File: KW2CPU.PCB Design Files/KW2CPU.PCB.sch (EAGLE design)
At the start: 67 parts, among them IC1 25AA080SN, J1 DF12_M, J2 MOLEX55560-0207, J3 MMCX_VERT, U1 MKW21D, U3 RF6555, U5 F-ANTENNA, X1 32KHZ, X2 32MHZ

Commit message: Added part numbers and manufacturers (inconsistent)
Also moved files to proper directories. Needs manual inconsistency
fixing
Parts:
- C1, C2, C3, C4: MFGN (none) -> Murata; MFGP (none) -> GRM1555C1H120JA01D
- C10, C13, C18, C7: MFGN (none) -> Murata; MFGP (none) -> GRM1555C1H5R0BA01D
- C11, C14, C17, C6: MFGN (none) -> Murata; MFGP (none) -> GRM155R71H102KA01D
- C12, C8: MFGN (none) -> Murata; MFGP (none) -> GRM155R61A334KE15D
- C15, C16, C19, C5: MFGN (none) -> Murata; MFGP (none) -> GRM155R71C104KA88D
- C20: value (none) -> 1.2pF
- C21, C28, C29, C30: value (none) -> 8pF
- C22: value (none) -> 1uF
- C23: value (none) -> 5.1pF
- C25: value (none) -> 0.2pF; MFGN (none) -> Johanson; MFGP (none) -> 500R07S0R2BV4T; NOTES DNP -> (none)
- C26: NOTE DNP -> (none); NOTES (none) -> DNP
- C9: MFGN (none) -> Murata; MFGP (none) -> GRM1555C1H330JA01D
- IC1: MFGN (none) -> Microchip; MFGP (none) -> 25AA640A; MPN (none) -> 25AA640A
- J1: MFGN (none) -> Hirose; MFGP (none) -> DF12(3.0)-40DS-0.5V(86)
- J2: MFGN (none) -> MOLEX; MFGP (none) -> 55560-0207
- L1, L2: value (none) -> 1nH
- L3: value (none) -> 100Ohm Ferrite
- L4: value (none) -> 2.2nH; MFGN (none) -> Murata; MFGP (none) -> LQP15MN2N2B02D
- L5: value (none) -> 0; MFGN (none) -> Panasonic; MFGP (none) -> ERJ-2GE0R00X
- R1: MFGN (none) -> Panasonic; MFGP (none) -> ERJ-2GEJ105X
- R10, R11, R12: MFGN (none) -> Panasonic; MFGP (none) -> ERJ-2RKF1002X
- R4, R5: value (none) -> 0
- R6: value (none) -> 51k
- R7, R9: value (none) -> 0; MFGP ERJ-2GEJ513X -> ERJ-2GE0R00X
- R8: value (none) -> 0; MFGP ERJ-2GEJ513X -> ERJ-2GE0R00X; NOTES (none) -> DNP
- TP1, TP10, TP11, TP12, TP2, TP3, TP4, TP5, TP6, TP7, TP8, TP9, U5: NOTES (none) -> DNP
- U1: MFGN (none) -> Freescale; MFGP (none) -> MKW21D256
- U4: MFGN (none) -> Microchip; MFGP (none) -> MCP1804T-3302I
- X1: MFGN (none) -> EPSON; MFGP (none) -> FC-135 32.7680KA-A3

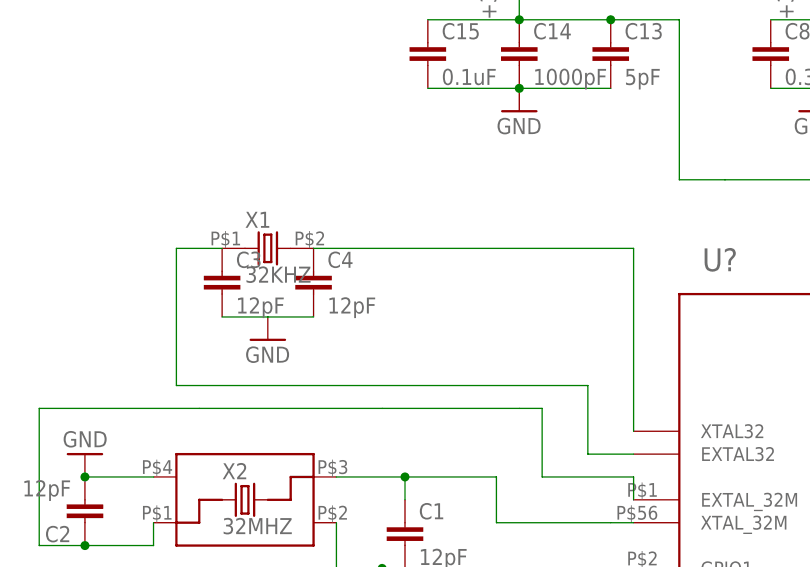
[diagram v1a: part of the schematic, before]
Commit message: Exporting production files in progress
Creating production files. Missing: ECO, Stackup, Drill
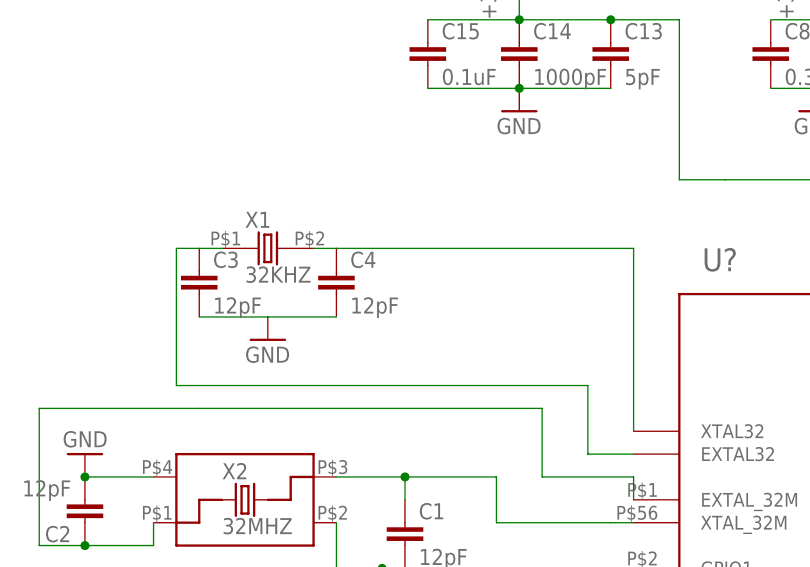
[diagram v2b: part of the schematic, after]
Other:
- moved on the sheet: C3, C4
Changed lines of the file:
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@@
 <attribute name="MFGP" x="-106.68" y="55.88" size="1.778" layer="96" display="off"/>
 </instance>
-<instance part="C3" gate="G$1" x="-111.76" y="53.34">
-<attribute name="MFGN" x="-111.76" y="53.34" size="1.778" layer="96" display="off"/>
-<attribute name="MFGP" x="-111.76" y="53.34" size="1.778" layer="96" display="off"/>
-</instance>
-<instance part="C4" gate="G$1" x="-101.6" y="53.34">
-<attribute name="MFGN" x="-101.6" y="53.34" size="1.778" layer="96" display="off"/>
-<attribute name="MFGP" x="-101.6" y="53.34" size="1.778" layer="96" display="off"/>
+<instance part="C3" gate="G$1" x="-114.3" y="53.34">
+<attribute name="MFGN" x="-114.3" y="53.34" size="1.778" layer="96" display="off"/>
+<attribute name="MFGP" x="-114.3" y="53.34" size="1.778" layer="96" display="off"/>
+</instance>
+<instance part="C4" gate="G$1" x="-99.06" y="53.34">
+<attribute name="MFGN" x="-99.06" y="53.34" size="1.778" layer="96" display="off"/>
+<attribute name="MFGP" x="-99.06" y="53.34" size="1.778" layer="96" display="off"/>
 </instance>
 <instance part="GND33" gate="1" x="-106.68" y="45.72"/>
@@
 <wire x1="-71.12" y1="40.64" x2="-116.84" y2="40.64" width="0.1524" layer="91"/>
 <wire x1="-116.84" y1="40.64" x2="-116.84" y2="55.88" width="0.1524" layer="91"/>
-<wire x1="-116.84" y1="55.88" x2="-111.76" y2="55.88" width="0.1524" layer="91"/>
+<wire x1="-116.84" y1="55.88" x2="-114.3" y2="55.88" width="0.1524" layer="91"/>
+<wire x1="-114.3" y1="55.88" x2="-111.76" y2="55.88" width="0.1524" layer="91"/>
 </segment>
 </net>
@@
 <pinref part="X1" gate="G$1" pin="2"/>
 <pinref part="C4" gate="G$1" pin="1"/>
-<wire x1="-101.6" y1="55.88" x2="-66.04" y2="55.88" width="0.1524" layer="91"/>
+<wire x1="-99.06" y1="55.88" x2="-66.04" y2="55.88" width="0.1524" layer="91"/>
 <pinref part="U1" gate="G$1" pin="XTAL32"/>
 <wire x1="-66.04" y1="55.88" x2="-66.04" y2="35.56" width="0.1524" layer="91"/>
+<wire x1="-99.06" y1="55.88" x2="-101.6" y2="55.88" width="0.1524" layer="91"/>
 </segment>
 </net>
@@
 <pinref part="GND33" gate="1" pin="GND"/>
 <pinref part="C4" gate="G$1" pin="2"/>
-<wire x1="-106.68" y1="48.26" x2="-101.6" y2="48.26" width="0.1524" layer="91"/>
+<wire x1="-106.68" y1="48.26" x2="-99.06" y2="48.26" width="0.1524" layer="91"/>
 <pinref part="C3" gate="G$1" pin="2"/>
-<wire x1="-106.68" y1="48.26" x2="-111.76" y2="48.26" width="0.1524" layer="91"/>
+<wire x1="-106.68" y1="48.26" x2="-114.3" y2="48.26" width="0.1524" layer="91"/>
 </segment>
 <segment>
@@
 </sheet>
 </sheets>
+<errors>
+</errors>
 </schematic>
 </drawing>

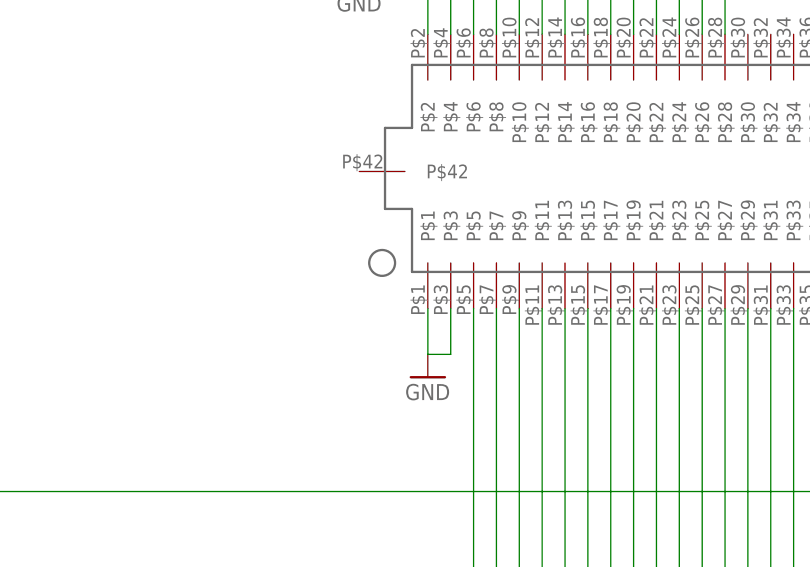
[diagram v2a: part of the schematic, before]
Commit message: KW2CPU.PCB.v1.1 Release
Fixed Gerbers (omitted layer), fixed BOM suffixes (see ECO), tented vias
and antenna holes in Eagle (and Gerbers), added Stackup -> Layer in Fab
notes.
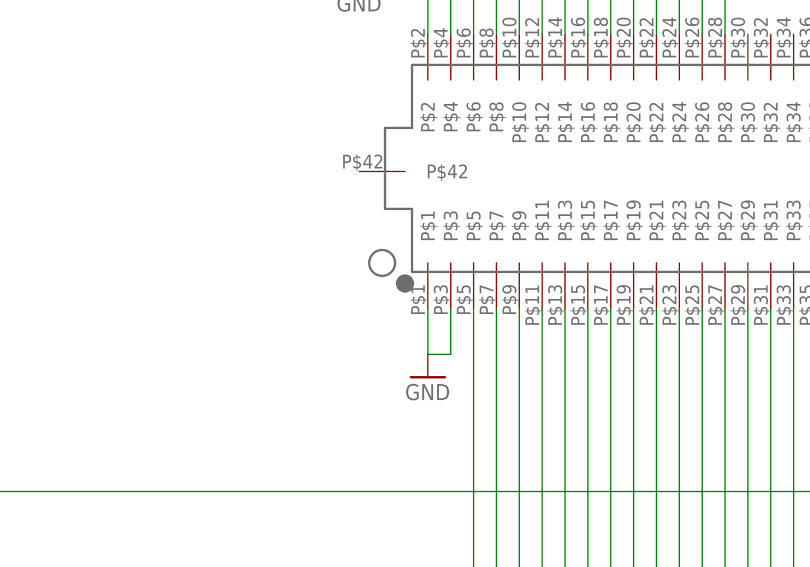
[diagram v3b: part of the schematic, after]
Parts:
- IC1: MFGP 25AA640A -> 25AA640A-I/SN
- U1: MFGP MKW21D256 -> MKW21D256VHA5
- U4: MFGP MCP1804T-3302I -> MCP1804T-3302I/DB
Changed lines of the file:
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@@
 <part name="U1" library="ZIGBEE" deviceset="MKW21D" device="">
 <attribute name="MFGN" value="Freescale"/>
-<attribute name="MFGP" value="MKW21D256"/>
+<attribute name="MFGP" value="MKW21D256VHA5"/>
 </part>
 <part name="GND1" library="supply1" deviceset="GND" device=""/>
@@
 <part name="U4" library="microchip" deviceset="MCP1804T-3302I" device="">
 <attribute name="MFGN" value="Microchip"/>
-<attribute name="MFGP" value="MCP1804T-3302I"/>
+<attribute name="MFGP" value="MCP1804T-3302I/DB"/>
 </part>
 <part name="+3V9" library="supply1" deviceset="+3V3" device=""/>
@@
 <part name="IC1" library="microchip" deviceset="25*" device="SN" technology="AA080">
 <attribute name="MFGN" value="Microchip"/>
-<attribute name="MFGP" value="25AA640A"/>
+<attribute name="MFGP" value="25AA640A-I/SN"/>
 <attribute name="MPN" value="25AA640A"/>
 <attribute name="OC_FARNELL" value=""/>

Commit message: Fixed PTC5 net name
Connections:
- net PTC5/LLWU_P8/SPI0_PCS0/UART1_TX/FTM0_CH3/CMP1_OUT renamed PTC5/LLWU_P9/SPI0_SCK/LPTMR0_ALT2/I2S0_RXDO/CMP0_OUT
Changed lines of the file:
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@@
 </segment>
 </net>
-<net name="PTC5/LLWU_P8/SPI0_PCS0/UART1_TX/FTM0_CH3/CMP1_OUT" class="0">
+<net name="PTC5/LLWU_P9/SPI0_SCK/LPTMR0_ALT2/I2S0_RXDO/CMP0_OUT" class="0">
 <segment>
 <pinref part="U1" gate="G$1" pin="PTC5/LLWU_P9/SPI0_SCK/LPTMR0_ALT2/I2S0_RXDO/CMP0_OUT"/>

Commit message: KW2CPU.PCB.v1.2 Release
DNP Voltage regulator (BOM change + schematic attribute, ECO),
incremented silkscreen to v1.2, fixed name on BOM filr (added .BOM)
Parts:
- U4: NOTES (none) -> DNP
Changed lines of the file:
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@@
 <attribute name="MFGN" value="Microchip"/>
 <attribute name="MFGP" value="MCP1804T-3302I/DB"/>
+<attribute name="NOTES" value="DNP"/>
 </part>
 <part name="+3V9" library="supply1" deviceset="+3V3" device=""/>
@@
 <attribute name="MFGN" x="243.84" y="-63.5" size="1.778" layer="96" display="off"/>
 <attribute name="MFGP" x="243.84" y="-63.5" size="1.778" layer="96" display="off"/>
+<attribute name="NOTES" x="243.84" y="-63.5" size="1.778" layer="96" display="off"/>
 </instance>
 <instance part="+3V9" gate="G$1" x="259.08" y="-55.88" smashed="yes">

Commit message: First cut at v1.3 (antenna diversity)
* Antenna diversity
* ISO layouts
* More TPs
* Axial anchors
* Remvoe top JTAG connector
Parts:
- removed J2: MOLEX55560-0207, KW2:MOLEX55560-0207
- removed J3: MMCX_VERT, KW2:MMCX_VERT
- removed U5: F-ANTENNA, KW2:F-ANTENNA
- added A1, A2: (no value), adafruit:ANTENNA_U.FL
- added TP13, TP14, TP15, TP16, TP17: PTR1TP15R, testpad:PTR1TP15R
- added U$1: CODESHELF-LOGOSMALL, GW-devices:CODESHELF-LOGOSMALL
- C24, C26, C27: value (none) -> 0pF
- L5: value 0 -> 0nH
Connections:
- removed net F_ANT: C24.1, L4.2, U5.IN
- removed net MMCX_ANT: C27.1, J3.P$1, L5.1
- new net U.FL.ANT1: A1.SIGNAL, C24.1, L4.2
- new net U.FL.ANT2: A2.SIGNAL, C27.1, L5.1
- net !RESET: no longer J2.P$10
- net +3V3: no longer J2.P$1
- net GND: now also A1.GND@0, A1.GND@1, A2.GND@0, A2.GND@1; no longer J2.P$15, J2.P$17, J2.P$19, J2.P$3, J2.P$5, J2.P$9, J3.P$2, J3.P$3, J3.P$4, J3.P$5, U5.GND
- net PTA0/JTAG_TCLK/SWD_CLK/EZP_CLK/!UART0_CTS/!UART0_COL/FTM0_CH5: no longer J2.P$4
- net PTA1/JTAG_TDI/EZP_DI/UART0/RX/FTM0_CH6: no longer J2.P$8
- net PTA2/JTAG_TDO/TRACE?SWO/EZP_DO/UART0_TX/FTM0_CH7: no longer J2.P$6
- net PTA3/JTAG_TMS/SWD_DIO/UART0_RTS/FTM0_CH0: no longer J2.P$2
- net PTC4/LLWU_P8/SPI0_PCS0/UART1_TX/FTM0_CH3/CMP1_OUT: now also TP13.TP
- net PTC5/LLWU_P9/SPI0_SCK/LPTMR0_ALT2/I2S0_RXDO/CMP0_OUT: now also TP14.TP
- net PTE0/MADC0_SE10/SPI1_PCS1/UART1_TX/MTRACE_CLKOUT/I2C1_SDA/RTC_CLKOUT: now also TP15.TP; no longer J2.P$12
- net PTE1/LLWU_P0/MADC0_SE11/SPI1_SOUT/UART1_RX/MTRACE_D3/I2C1_SCL/SPI1_SIN: now also TP16.TP; no longer J2.P$20
- net PTE2/LLWU_P1/MADC0_DP1/SPI1_SCK/!UART1_CTS!/MTRACE_D2: no longer J2.P$18
- net PTE3/MADC0_DM1/SPI1_SIN/!UART1_RTS!/MTRACE_D1/SPI1_SOUT: now also TP17.TP; no longer J2.P$16
- net PTE4/LLWU_P2/SPI1_PCS0/MTRACE_D0: no longer J2.P$14
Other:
- moved on the sheet: C20, C21, C22, C23, C24, C25, C26, C27, C29, C30, L1, L2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

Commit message: KW2 v1.3 revisions
The first big slug of KW2 revisions.
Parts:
- added R2: 0, GW-devices:RF-RRFMD
- added RFI1, RFI2, RFI3, RFI4, RFI5, RFI6, TP18: PTR1TP15R, testpad:PTR1TP15R
- C1, C2: value 12pF -> 9pF; MFGP GRM1555C1H120JA01D -> GRM1555C1H9R0DA01D
- C24: value 0pF -> 0.5pF
- C25: value 0.2pF -> 0.0pF
- C26: value 0pF -> 1.0pF
- L4: value 2.2nH -> 1.2nH
- L5: value 0nH -> 1.5nH
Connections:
- removed net C_LNA: R7.1, R8.2, U3.C_LNA
- new net GPIO1: J1.P$30, U1.GPIO1
- new net GPIO2: J1.P$32, R7.1, R8.2, U1.GPIO2, U3.C_LNA
- net ANTSEL: now also R2.1
- net GND: now also RFI1.TP, RFI2.TP, RFI3.TP, RFI4.TP, RFI5.TP, RFI6.TP
- net PTE2/LLWU_P1/MADC0_DP1/SPI1_SCK/!UART1_CTS!/MTRACE_D2: now also TP17.TP
- net PTE3/MADC0_DM1/SPI1_SIN/!UART1_RTS!/MTRACE_D1/SPI1_SOUT: now also TP18.TP; no longer TP17.TP
- net TX_SWITCH: now also R2.2
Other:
- moved on the sheet: C1, C2, C28, C3, C4, R1, X1, X2
